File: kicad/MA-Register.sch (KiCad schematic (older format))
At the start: 0 parts

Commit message: Finish todo list
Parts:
- added U? (x2): 74LS245, symbol 74xx:74LS245
- added U? (x4): 74LS173, symbol 74xx:74LS173
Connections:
- net BUS_0: now also U?.11 (B7), U?.11 (D3)
- net BUS_1: now also U?.12 (B6), U?.12 (D2)
- net BUS_10: now also U?.13 (B5), U?.13 (D1)
- net BUS_11: now also U?.14 (B4), U?.14 (D0)
- net BUS_12: now also U?.11 (D3), U?.15 (B3)
- net BUS_13: now also U?.12 (D2), U?.16 (B2)
- net BUS_14: now also U?.13 (D1), U?.17 (B1)
- net BUS_15: now also U?.14 (D0), U?.18 (B0)
- net BUS_2: now also U?.13 (B5), U?.13 (D1)
- net BUS_3: now also U?.14 (B4), U?.14 (D0)
- net BUS_4: now also U?.11 (D3), U?.15 (B3)
- net BUS_5: now also U?.12 (D2), U?.16 (B2)
- net BUS_6: now also U?.13 (D1), U?.17 (B1)
- net BUS_7: now also U?.14 (D0), U?.18 (B0)
- net BUS_8: now also U?.11 (B7), U?.11 (D3)
- net BUS_9: now also U?.12 (B6), U?.12 (D2)
- net RAM_0: now also U?.5 (A3), U?.6 (Q3)
- net RAM_1: now also U?.4 (A2), U?.5 (Q2)
- net RAM_10: now also U?.3 (A1), U?.4 (Q1)
- net RAM_11: now also U?.2 (A0), U?.3 (Q0)
- net RAM_12: now also U?.6 (Q3), U?.9 (A7)
- net RAM_13: now also U?.5 (Q2), U?.8 (A6)
- net RAM_14: now also U?.4 (Q1), U?.7 (A5)
- net RAM_15: now also U?.3 (Q0), U?.6 (A4)
- net RAM_2: now also U?.3 (A1), U?.4 (Q1)
- net RAM_3: now also U?.2 (A0), U?.3 (Q0)
- net RAM_4: now also U?.6 (Q3), U?.9 (A7)
- net RAM_5: now also U?.5 (Q2), U?.8 (A6)
- net RAM_6: now also U?.4 (Q1), U?.7 (A5)
- net RAM_7: now also U?.3 (Q0), U?.6 (A4)
- net RAM_8: now also U?.5 (A3), U?.6 (Q3)
- net RAM_9: now also U?.4 (A2), U?.5 (Q2)
- new net CLK: U?.7 (Cp), U?.7 (Cp), U?.7 (Cp), U?.7 (Cp)
- new net CLR: U?.15 (Mr), U?.15 (Mr), U?.15 (Mr), U?.15 (Mr)
- new net GND: U?.1 (Oe1), U?.1 (Oe1), U?.1 (Oe1), U?.1 (Oe1), U?.2 (Oe2), U?.2 (Oe2), U?.2 (Oe2), U?.2 (Oe2)
- new net VCC: U?.1 (A->B), U?.1 (A->B)
- new net ~MAI~: U?.10 (E2), U?.10 (E2), U?.10 (E2), U?.10 (E2), U?.9 (E1), U?.9 (E1), U?.9 (E1), U?.9 (E1)
- new net ~MAO~: U?.19 (CE), U?.19 (CE)

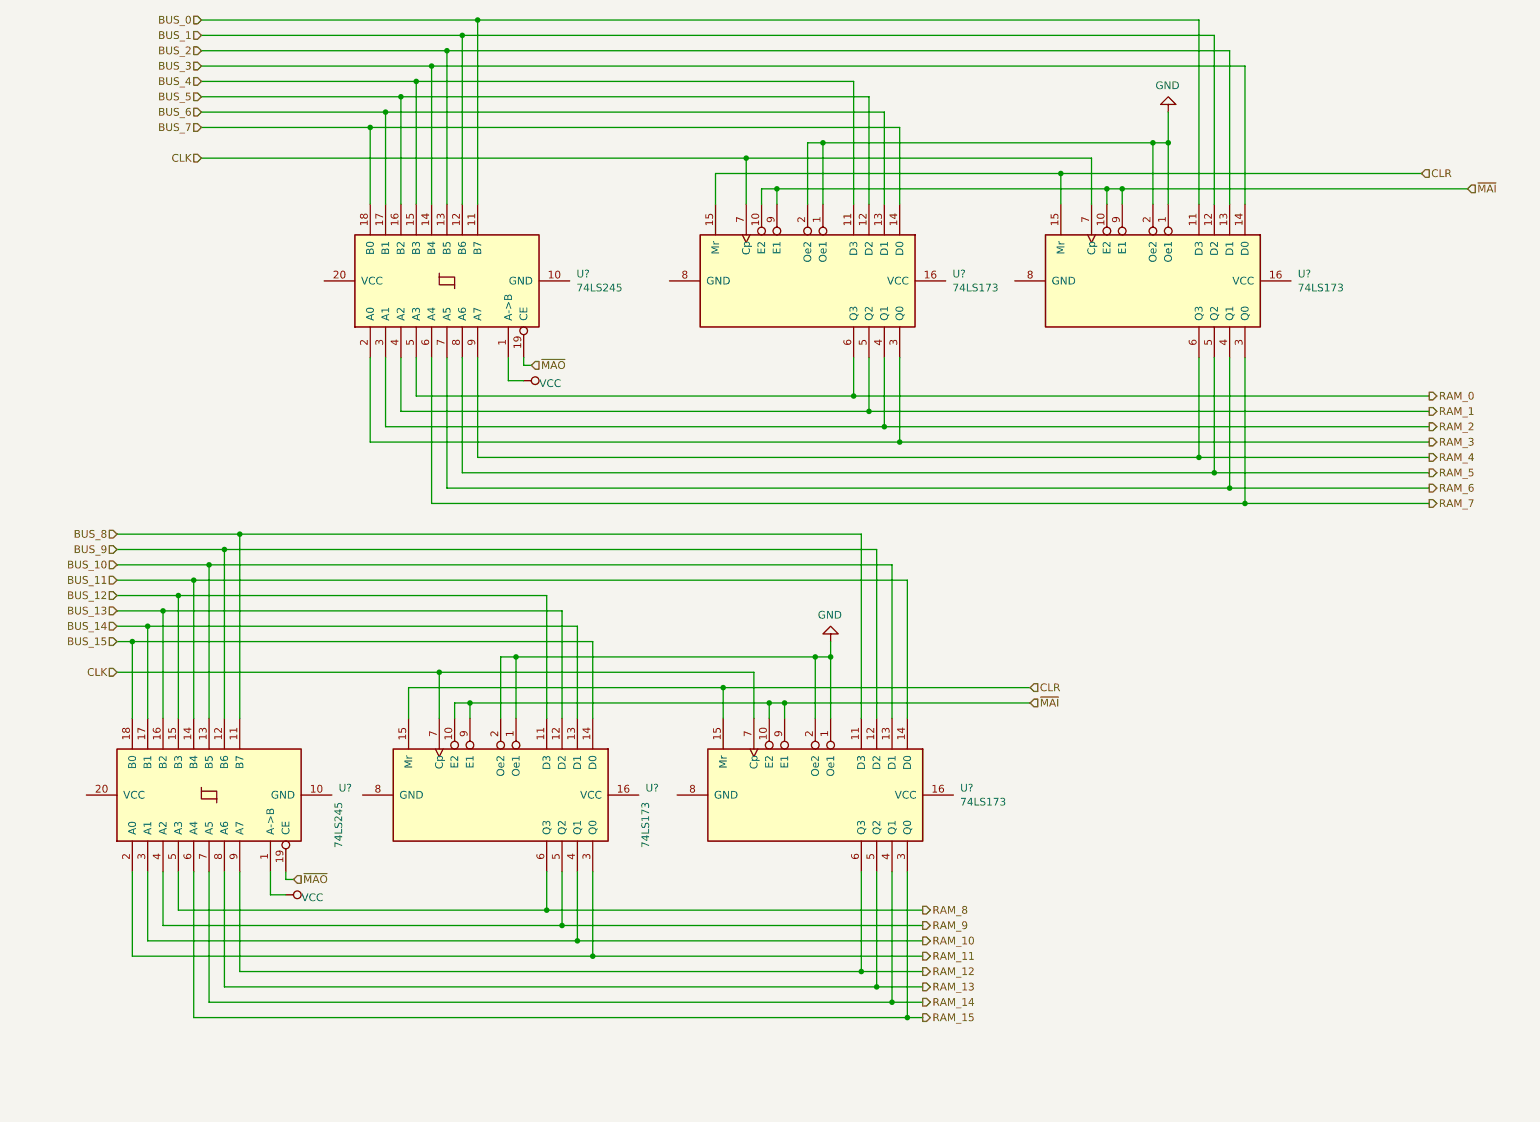
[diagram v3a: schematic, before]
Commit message: Reorganize part references
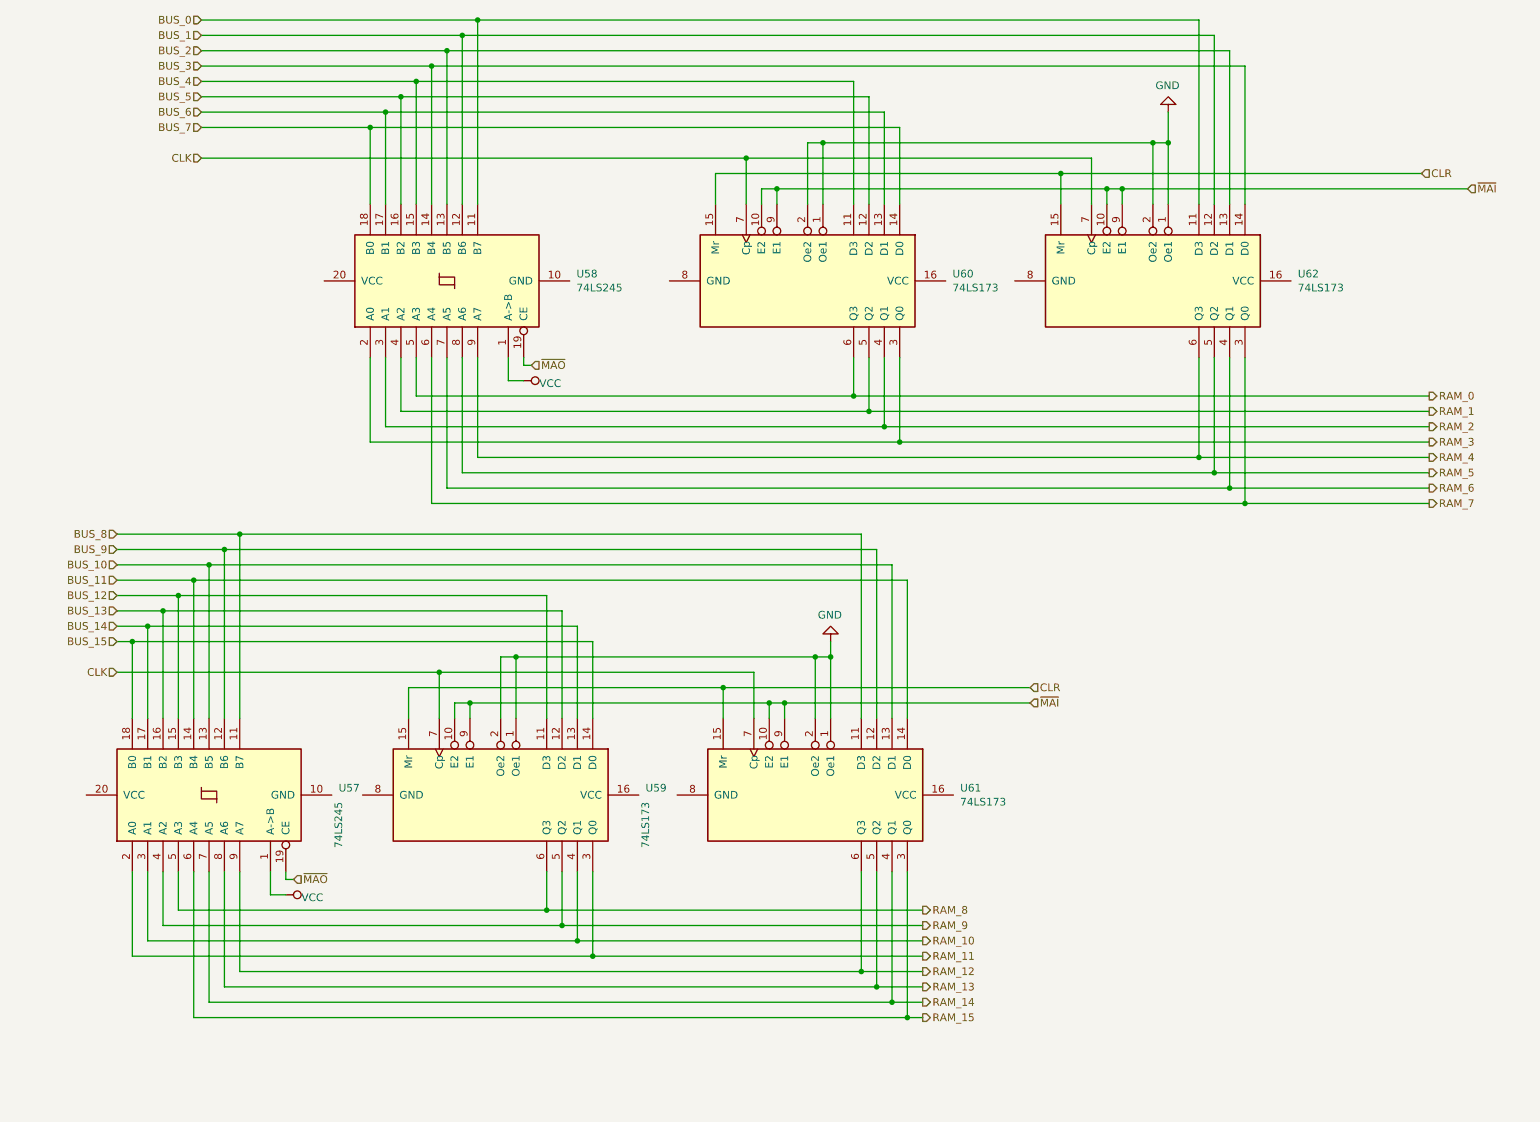
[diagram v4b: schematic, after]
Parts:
- gave numbers to parts that had none: 6
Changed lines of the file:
@@
 AR Path="/5DA98D6D/5DA9A5B3/5E64EBBE" Ref="U?"  Part="1"
 AR Path="/5DA9B7A7/5E64EBBE" Ref="U?"  Part="1"
-AR Path="/5E5B2276/5D807A05/5E64EBBE" Ref="U?"  Part="1"
-F 0 "U?" V 3446 1656 50  0000 R CNN
+AR Path="/5E5B2276/5D807A05/5E64EBBE" Ref="U58"  Part="1"
+F 0 "U58" V 3446 1656 50  0000 R CNN
 F 1 "74LS245" V 3355 1656 50  0000 R CNN
 F 2 "" H 3400 2500 50  0001 C CNN
@@
 AR Path="/5DA98D6D/5DA9A5B3/5E64EBEB" Ref="U?"  Part="1"
 AR Path="/5DA9B7A7/5E64EBEB" Ref="U?"  Part="1"
-AR Path="/5E5B2276/5D807A05/5E64EBEB" Ref="U?"  Part="1"
-F 0 "U?" V 7954 3444 50  0000 L CNN
+AR Path="/5E5B2276/5D807A05/5E64EBEB" Ref="U62"  Part="1"
+F 0 "U62" V 7954 3444 50  0000 L CNN
 F 1 "74LS173" V 8045 3444 50  0000 L CNN
 F 2 "" H 8000 2500 50  0001 C CNN
@@
 AR Path="/5DA98D6D/5DA9A5B3/5E64ECD6" Ref="U?"  Part="1"
 AR Path="/5DA9B7A7/5E64ECD6" Ref="U?"  Part="1"
-AR Path="/5E5B2276/5D807A05/5E64ECD6" Ref="U?"  Part="1"
-F 0 "U?" V 5704 3444 50  0000 L CNN
+AR Path="/5E5B2276/5D807A05/5E64ECD6" Ref="U60"  Part="1"
+F 0 "U60" V 5704 3444 50  0000 L CNN
 F 1 "74LS173" V 5795 3444 50  0000 L CNN
 F 2 "" H 5750 2500 50  0001 C CNN
@@
 AR Path="/5DA98D6D/5DA9A5B3/5E69CBF9" Ref="U?"  Part="1"
 AR Path="/5DA9B7A7/5E69CBF9" Ref="U?"  Part="1"
-AR Path="/5E5B2276/5D807A05/5E69CBF9" Ref="U?"  Part="1"
-F 0 "U?" V 3704 6794 50  0000 L CNN
+AR Path="/5E5B2276/5D807A05/5E69CBF9" Ref="U59"  Part="1"
+F 0 "U59" V 3704 6794 50  0000 L CNN
 F 1 "74LS173" H 3795 6794 50  0000 L CNN
 F 2 "" H 3750 5850 50  0001 C CNN
@@
 AR Path="/5DA98D6D/5DA9A5B3/5E69CB0E" Ref="U?"  Part="1"
 AR Path="/5DA9B7A7/5E69CB0E" Ref="U?"  Part="1"
-AR Path="/5E5B2276/5D807A05/5E69CB0E" Ref="U?"  Part="1"
-F 0 "U?" V 5754 6794 50  0000 L CNN
+AR Path="/5E5B2276/5D807A05/5E69CB0E" Ref="U61"  Part="1"
+F 0 "U61" V 5754 6794 50  0000 L CNN
 F 1 "74LS173" V 5845 6794 50  0000 L CNN
 F 2 "" H 5800 5850 50  0001 C CNN
@@
 AR Path="/5DA98D6D/5DA9A5B3/5E69CAE1" Ref="U?"  Part="1"
 AR Path="/5DA9B7A7/5E69CAE1" Ref="U?"  Part="1"
-AR Path="/5E5B2276/5D807A05/5E69CAE1" Ref="U?"  Part="1"
-F 0 "U?" V 1896 5006 50  0000 R CNN
+AR Path="/5E5B2276/5D807A05/5E69CAE1" Ref="U57"  Part="1"
+F 0 "U57" V 1896 5006 50  0000 R CNN
 F 1 "74LS245" H 1805 5006 50  0000 R CNN
 F 2 "" H 1850 5850 50  0001 C CNN

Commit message: Up to v1.0 and plot
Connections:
- net RAM_14 is gone; now on net RAM_10: U57.7 (A5), U61.4 (Q1)
- net RAM_15 is gone; now on net RAM_11: U57.6 (A4), U61.3 (Q0)
- net RAM_8 is gone; now on net RAM_12: U57.5 (A3), U59.6 (Q3)
- net RAM_9 is gone; now on net RAM_13: U57.4 (A2), U59.5 (Q2)
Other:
- moved on the sheet: U57, U58, U59, U60, U61, U62
